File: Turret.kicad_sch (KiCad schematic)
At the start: 24 parts, among them J1 Conn_01x04_Pin, J10 Conn_01x04_Pin, J11 Sabre Vertical Header 6, J12 Conn_01x02_Pin, J13 Conn_01x04_Pin, J14 Conn_01x04_Pin, J15 Conn_01x08_Pin, J2 Conn_01x02_Pin, J20 Conn_01x02_Pin, J21 Conn_01x02_Pin, J3 Conn_01x02_Pin, J4 Conn_01x02_Pin, J5 Conn_01x04_Pin, J6 Conn_01x02_Pin, J7 Conn_01x02_Pin, J8 Conn_01x02_Pin, J9 Conn_01x02_Pin

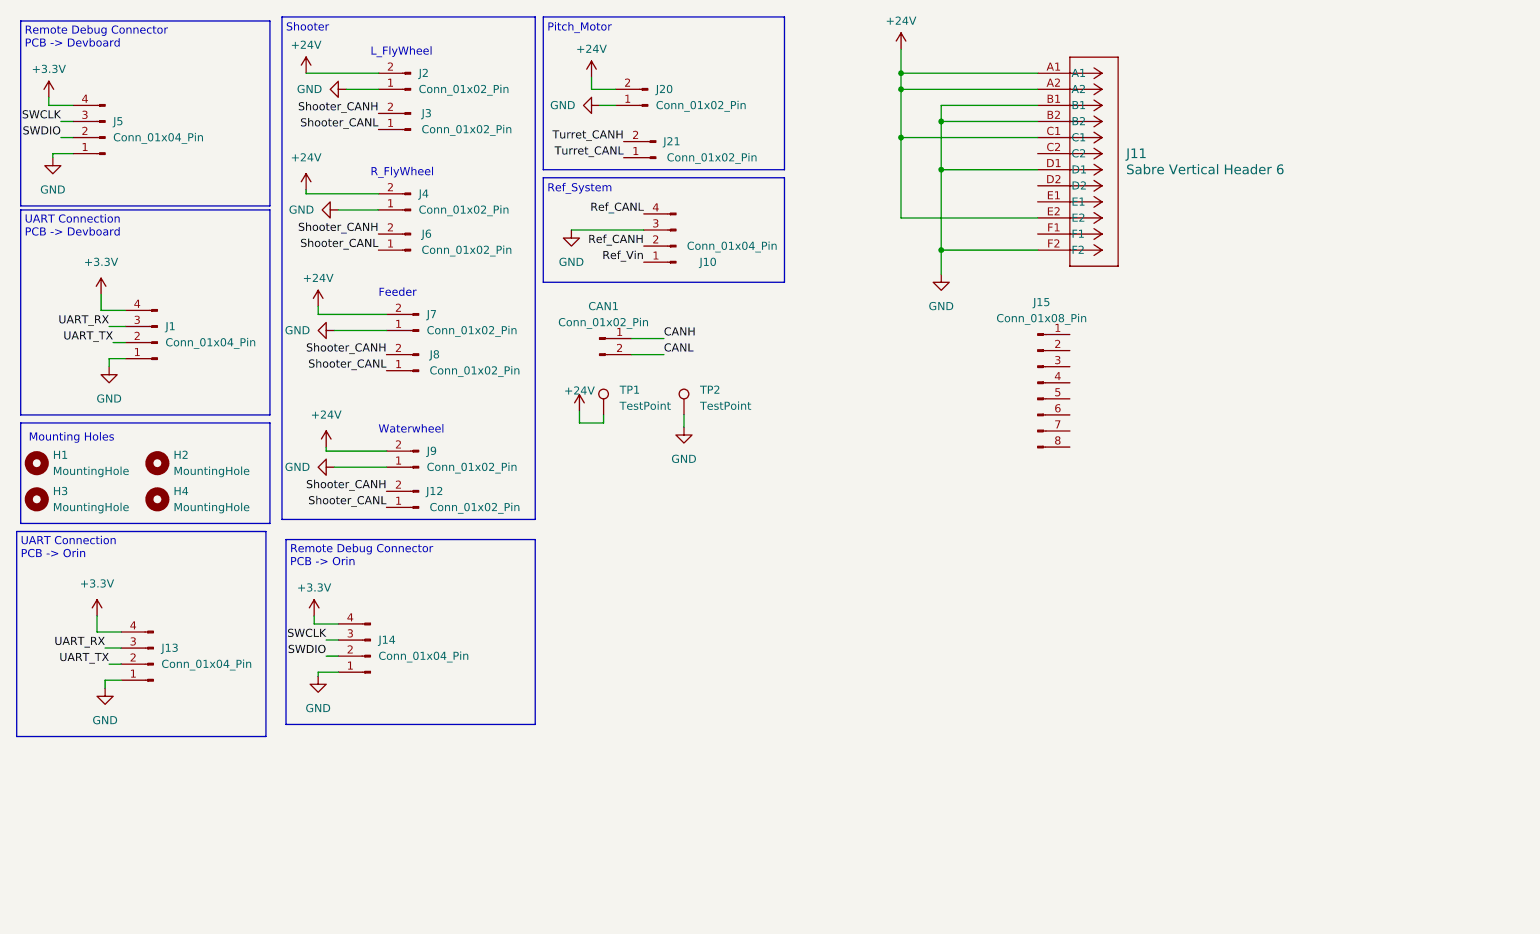
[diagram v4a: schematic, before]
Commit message: Added 8 pin, ref system connection not needed?
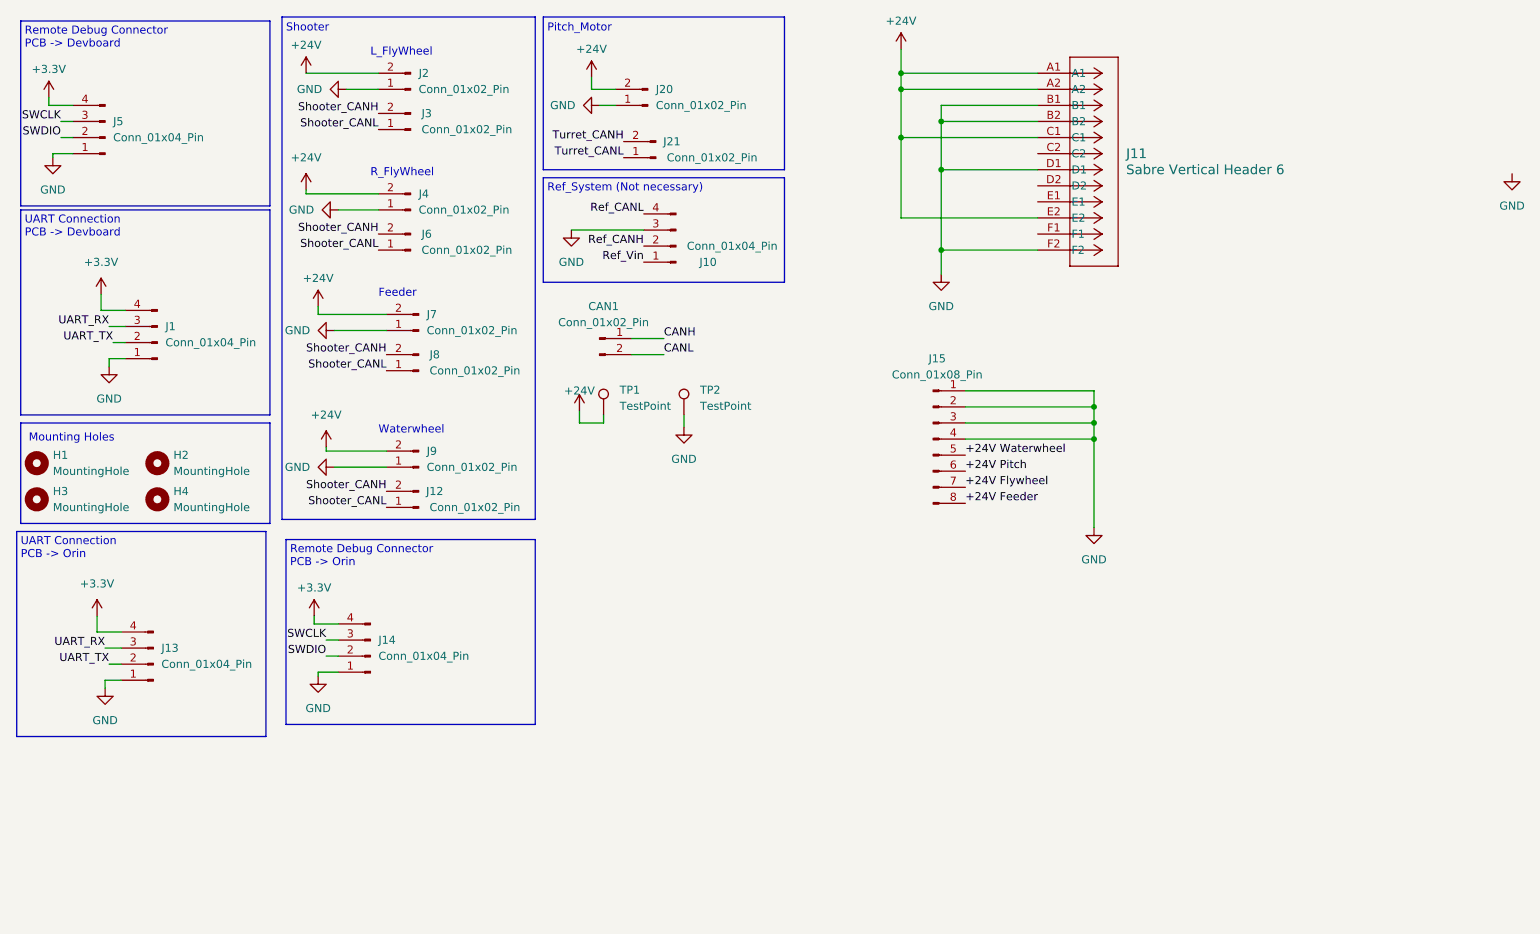
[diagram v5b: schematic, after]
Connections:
- net GND: now also J15.1 (Pin_1), J15.2 (Pin_2), J15.3 (Pin_3), J15.4 (Pin_4)
- net +24V Waterwheel: now reaches J15.5 (Pin_5)
- net +24V Pitch: now reaches J15.6 (Pin_6)
- net +24V Flywheel: now reaches J15.7 (Pin_7)
- net +24V Feeder: now reaches J15.8 (Pin_8)
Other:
- note added: "Ref_System (Not necessary)"
- note removed: "Ref_System"
- moved on the sheet: J15
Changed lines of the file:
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@@
 (kicad_sch (version 20230121) (generator eeschema)
   (paper "A4")
+  (junction (at 191.77 91.44) (diameter 0) (color 0 0 0 0)
+  )
   (junction (at 161.29 36.195) (diameter 0) (color 0 0 0 0)
   )
   (junction (at 167.64 64.135) (diameter 0) (color 0 0 0 0)
   )
+  (junction (at 191.77 88.9) (diameter 0) (color 0 0 0 0)
+  )
   (junction (at 167.64 51.435) (diameter 0) (color 0 0 0 0)
   )
@@
   (junction (at 161.29 46.355) (diameter 0) (color 0 0 0 0)
   )
+  (junction (at 191.77 93.98) (diameter 0) (color 0 0 0 0)
+  )
   (wire (pts (xy 28.575 46.355) (xy 30.48 46.355))
     (stroke (width 0) (type default))
@@
     (stroke (width 0) (type default))
   )
+  (wire (pts (xy 191.77 91.44) (xy 191.77 93.98))
+    (stroke (width 0) (type default))
+  )
   (wire (pts (xy 36.195 129.54) (xy 38.1 129.54))
     (stroke (width 0) (type default))
@@
     (stroke (width 0) (type default))
   )
+  (wire (pts (xy 191.77 88.9) (xy 191.77 91.44))
+    (stroke (width 0) (type default))
+  )
   (wire (pts (xy 112.395 36.83) (xy 112.395 38.735))
     (stroke (width 0) (type default))
@@
     (stroke (width 0) (type default))
   )
+  (wire (pts (xy 171.45 88.9) (xy 191.77 88.9))
+    (stroke (width 0) (type default))
+  )
   (wire (pts (xy 28.575 43.815) (xy 30.48 43.815))
     (stroke (width 0) (type default))
@@
     (stroke (width 0) (type default))
   )
+  (wire (pts (xy 191.77 86.36) (xy 191.77 88.9))
+    (stroke (width 0) (type default))
+  )
   (wire (pts (xy 35.56 132.08) (xy 35.56 133.35))
     (stroke (width 0) (type default))
@@
     (stroke (width 0) (type default))
   )
+  (wire (pts (xy 171.45 86.36) (xy 191.77 86.36))
+    (stroke (width 0) (type default))
+  )
   (wire (pts (xy 110.49 91.44) (xy 114.3 91.44))
     (stroke (width 0) (type default))
@@
     (stroke (width 0) (type default))
   )
+  (wire (pts (xy 191.77 93.98) (xy 171.45 93.98))
+    (stroke (width 0) (type default))
+  )
   (wire (pts (xy 182.88 59.055) (xy 161.29 59.055))
     (stroke (width 0) (type default))
@@
     (stroke (width 0) (type default))
   )
+  (wire (pts (xy 171.45 91.44) (xy 191.77 91.44))
+    (stroke (width 0) (type default))
+  )
   (wire (pts (xy 38.1 132.08) (xy 35.56 132.08))
     (stroke (width 0) (type default))
@@
     (stroke (width 0) (type default))
   )
+  (wire (pts (xy 191.77 93.98) (xy 191.77 107.95))
+    (stroke (width 0) (type default))
+  )
   (wire (pts (xy 110.49 89.535) (xy 110.49 91.44))
     (stroke (width 0) (type default))
@@
     (effects (font (size 1.27 1.27)) (justify left bottom))
   )
-  (text "Ref_System\n" (at 105.41 55.245 0)
+  (text "Ref_System (Not necessary)\n\n" (at 105.41 57.15 0)
     (effects (font (size 1.27 1.27)) (justify left bottom))
   )
@@
     (effects (font (size 1.27 1.27)) (justify left bottom))
   )
+  (label "+24V Feeder" (at 171.45 104.14 0) (fields_autoplaced)
+    (effects (font (size 1.27 1.27)) (justify left bottom))
+  )
   (label "Shooter_CANL" (at 78.74 45.085 180) (fields_autoplaced)
     (effects (font (size 1.27 1.27)) (justify right bottom))
@@
     (effects (font (size 1.27 1.27)) (justify right bottom))
   )
+  (label "+24V Pitch" (at 171.45 99.06 0) (fields_autoplaced)
+    (effects (font (size 1.27 1.27)) (justify left bottom))
+  )
   (label "Turret_CANH" (at 117.475 46.99 180) (fields_autoplaced)
     (effects (font (size 1.27 1.27)) (justify right bottom))
@@
     (effects (font (size 1.27 1.27)) (justify left bottom))
   )
+  (label "+24V Flywheel" (at 171.45 101.6 0) (fields_autoplaced)
+    (effects (font (size 1.27 1.27)) (justify left bottom))
+  )
   (label "UART_RX" (at 35.56 127 180) (fields_autoplaced)
     (effects (font (size 1.27 1.27)) (justify right bottom))
@@
   (label "Shooter_CANH" (at 78.74 61.595 180) (fields_autoplaced)
     (effects (font (size 1.27 1.27)) (justify right bottom))
+  )
+  (label "+24V Waterwheel" (at 171.45 96.52 0) (fields_autoplaced)
+    (effects (font (size 1.27 1.27)) (justify left bottom))
   )
   (label "SWDIO" (at 70.485 128.27 180) (fields_autoplaced)
@@
     )
   )
+  (symbol (lib_id "power:GND") (at 191.77 107.95 0) (unit 1)
+    (in_bom yes) (on_board yes) (dnp no) (fields_autoplaced)
+    (property "Reference" "#PWR024" (at 191.77 114.3 0)
+      (effects (font (size 1.27 1.27)) hide)
+    )
+    (property "Value" "GND" (at 191.77 113.03 0)
+      (effects (font (size 1.27 1.27)))
+    )
+    (property "Footprint" "" (at 191.77 107.95 0)
+      (effects (font (size 1.27 1.27)) hide)
+    )
+    (property "Datasheet" "" (at 191.77 107.95 0)
+      (effects (font (size 1.27 1.27)) hide)
+    )
+    (pin "1")
+    (instances
+      (project "Turret"
+        (path "/84905b3c-2997-4e61-b373-c0062fb72371"
+          (reference "#PWR024") (unit 1)
+        )
+      )
+    )
+  )
   (symbol (lib_id "power:GND") (at 72.39 57.785 270) (unit 1)
     (in_bom yes) (on_board yes) (dnp no) (fields_autoplaced)
@@
     )
   )
+  (symbol (lib_id "power:GND") (at 257.81 52.07 0) (unit 1)
+    (in_bom yes) (on_board yes) (dnp no) (fields_autoplaced)
+    (property "Reference" "#PWR025" (at 257.81 58.42 0)
+      (effects (font (size 1.27 1.27)) hide)
+    )
+    (property "Value" "GND" (at 257.81 57.15 0)
+      (effects (font (size 1.27 1.27)))
+    )
+    (property "Footprint" "" (at 257.81 52.07 0)
+      (effects (font (size 1.27 1.27)) hide)
+    )
+    (property "Datasheet" "" (at 257.81 52.07 0)
+      (effects (font (size 1.27 1.27)) hide)
+    )
+    (pin "1")
+    (instances
+      (project "Turret"
+        (path "/84905b3c-2997-4e61-b373-c0062fb72371"
+          (reference "#PWR025") (unit 1)
+        )
+      )
+    )
+  )
   (symbol (lib_id "power:GND") (at 109.22 60.96 0) (unit 1)
     (in_bom yes) (on_board yes) (dnp no) (fields_autoplaced)
@@
     )
   )
-  (symbol (lib_id "Connector:Conn_01x08_Pin") (at 182.88 85.09 0) (unit 1)
-    (in_bom yes) (on_board yes) (dnp no) (fields_autoplaced)
-    (property "Reference" "J15" (at 183.515 72.39 0)
-      (effects (font (size 1.27 1.27)))
-    )
-    (property "Value" "Conn_01x08_Pin" (at 183.515 74.93 0)
-      (effects (font (size 1.27 1.27)))
-    )
-    (property "Footprint" "" (at 182.88 85.09 0)
-      (effects (font (size 1.27 1.27)) hide)
-    )
-    (property "Datasheet" "~" (at 182.88 85.09 0)
-      (effects (font (size 1.27 1.27)) hide)
-    )
+  (symbol (lib_id "Connector:Conn_01x08_Pin") (at 166.37 93.98 0) (unit 1)
+    (in_bom yes) (on_board yes) (dnp no) (fields_autoplaced)
+    (property "Reference" "J15" (at 167.005 81.28 0)
+      (effects (font (size 1.27 1.27)))
+    )
+    (property "Value" "Conn_01x08_Pin" (at 167.005 83.82 0)
+      (effects (font (size 1.27 1.27)))
+    )
+    (property "Footprint" "" (at 166.37 93.98 0)
+      (effects (font (size 1.27 1.27)) hide)
+    )
+    (property "Datasheet" "~" (at 166.37 93.98 0)
+      (effects (font (size 1.27 1.27)) hide)
+    )

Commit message: Correct voltages
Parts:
- removed CAN1: Conn_01x02_Pin, Connector_JST:JST_GH_BM02B-GHS-TBT_1x02-1MP_P1.25mm_Vertical, symbol Connector:Conn_01x02_Pin
- removed J11: Sabre Vertical Header 6, symbol Robomaster_Library:Sabre Vertical Header 6
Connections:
- net +24V: no longer J2.2 (Pin_2), J20.2 (Pin_2), J4.2 (Pin_2), J7.2 (Pin_2), J9.2 (Pin_2)
- net +24V Feeder renamed +5V
- net +24V Flywheel renamed +19V
- net +24V Pitch renamed +24V Gimbal
- net +24V Gimbal: now also J20.2 (Pin_2)
- net +24V Waterwheel renamed +24V Shooter
- net +24V Shooter: now also J2.2 (Pin_2), J4.2 (Pin_2), J7.2 (Pin_2), J9.2 (Pin_2)
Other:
- note added: "Remote Debug Connector Orin -> Turret"
- note added: "Remote Debug Connector Turret -> Chassis"
- note added: "UART Connection Chassis -> Turret"
- note added: "UART Connection Turret -> Orin"
- note removed: "Remote Debug Connector PCB -> Devboard"
- note removed: "Remote Debug Connector PCB -> Orin"
- note removed: "UART Connection PCB -> Devboard"
- note removed: "UART Connection PCB -> Orin"
- moved on the sheet: H1, H2, H3, H4, J1, J10, J13, J15, J20, J21, J5

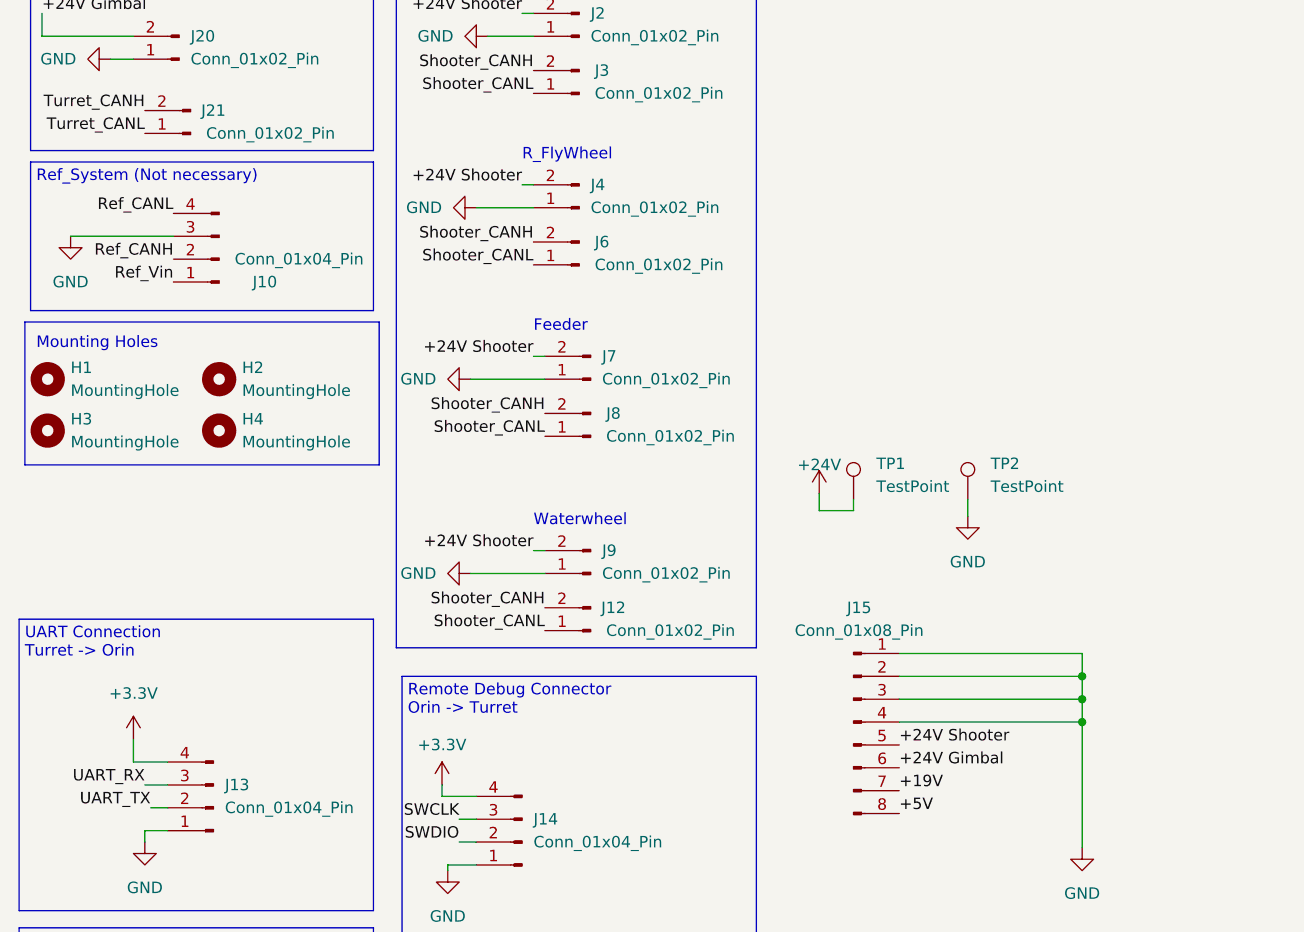
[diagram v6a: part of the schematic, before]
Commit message: Add footprints
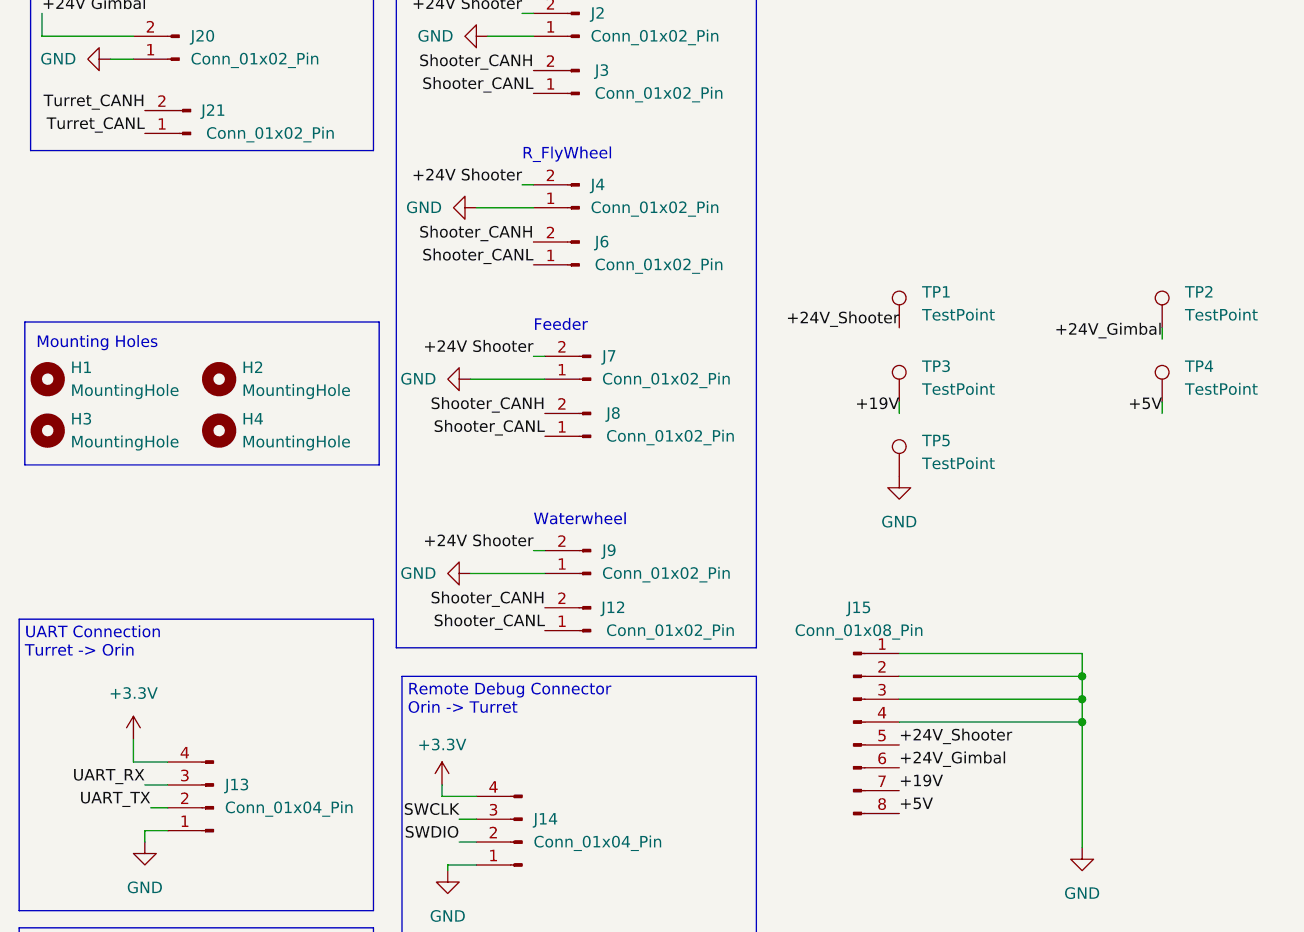
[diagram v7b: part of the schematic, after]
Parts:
- removed J10: Conn_01x04_Pin, ICs:866319112100004, symbol Connector:Conn_01x04_Pin
- added TP3, TP4, TP5: TestPoint, TestPoint:TestPoint_Loop_D1.80mm_Drill1.0mm_Beaded, symbol Connector:TestPoint
- J15: footprint (none) -> ICs:CON_1722981108_MOL
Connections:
- net +19V: now also TP3.1
- net +24V Gimbal: no longer J15.6 (Pin_6)
- net +24V Shooter: no longer J15.5 (Pin_5)
- net +5V: now also TP4.1
- net GND: now also TP5.1; no longer TP2.1
- net +24V renamed +24V_Shooter
- net +24V_Shooter: now also J15.5 (Pin_5)
- new net +24V_Gimbal: J15.6 (Pin_6), TP2.1
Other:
- note removed: "Ref_System (Not necessary)"
- moved on the sheet: TP1
